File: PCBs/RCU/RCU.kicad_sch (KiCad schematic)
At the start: 0 parts

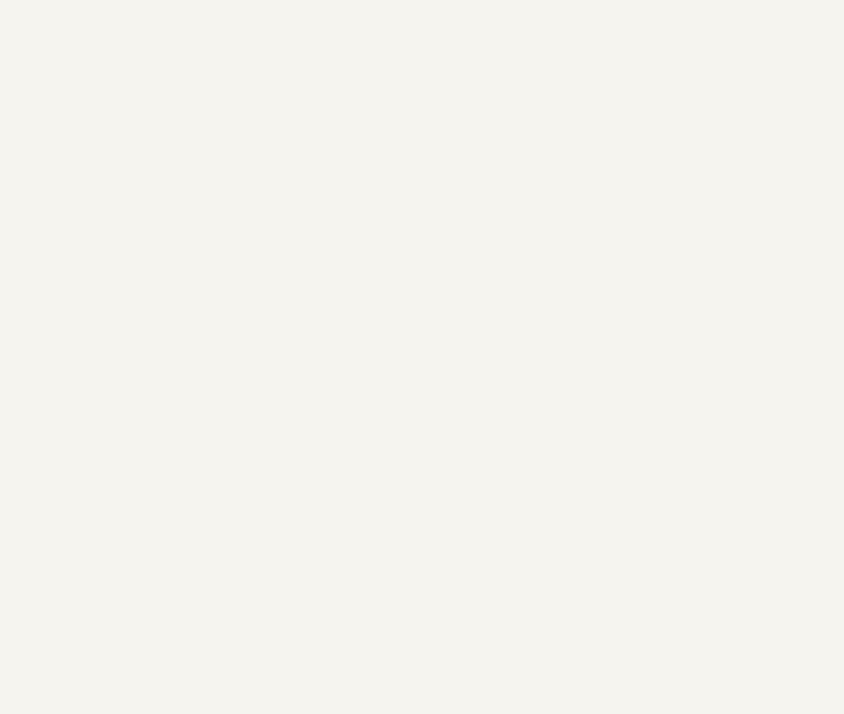
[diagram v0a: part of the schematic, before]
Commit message: Updated microcontroller schematic and created motor_control schematic
Changed all the net lables to global lavels except for NRST and USB_, added crystal resonator circuit, created DRV8876 symbol and added control signals to it
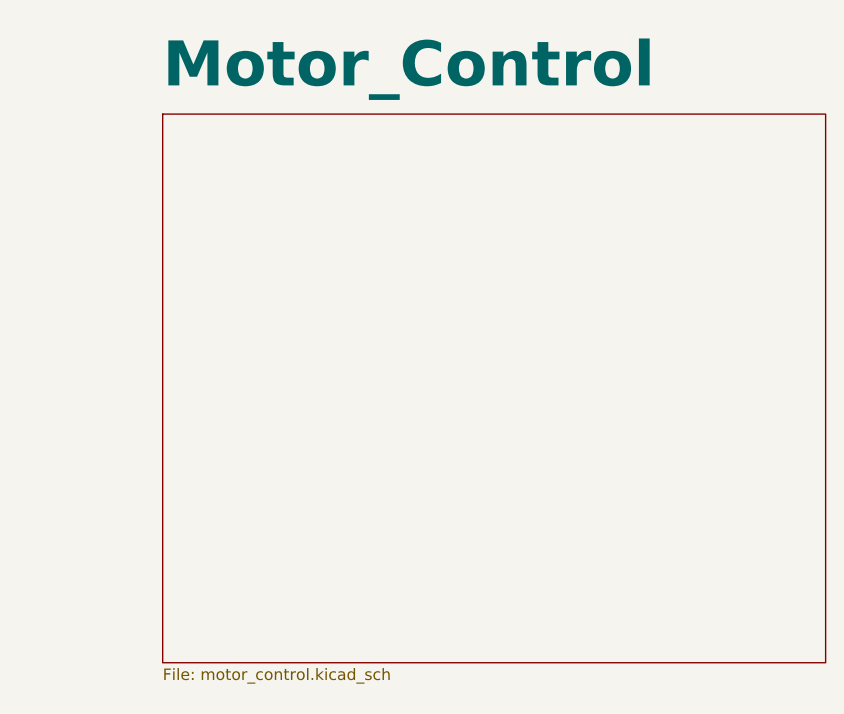
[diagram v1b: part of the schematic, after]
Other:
- added sheet Motor_Control (motor_control.kicad_sch)
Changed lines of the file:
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@@
 (kicad_sch (version 20211123) (generator eeschema)
   (paper "A4")
+  (sheet (at 139.7 26.67) (size 73.66 60.96) (fields_autoplaced)
+    (stroke (width 0.1524) (type solid) (color 0 0 0 0))
+    (fill (color 0 0 0 0.0000))
+    (property "Sheet name" "Motor_Control" (id 0) (at 139.7 24.0934 0)
+      (effects (font (size 5 5) bold) (justify left bottom))
+    )
+    (property "Sheet file" "motor_control.kicad_sch" (id 1) (at 139.7 88.2146 0)
+      (effects (font (size 1.27 1.27)) (justify left top))
+    )
+  )
   (sheet (at 33.7312 26.8732) (size 71.0184 61.722) (fields_autoplaced)
     (stroke (width 0.1524) (type solid) (color 0 0 0 0))
@@
     (path "/" (page "1"))
     (path "/c46a482e-bfa4-4ed5-a49f-3179709c39a1" (page "2"))
+    (path "/2537d888-fd78-4661-a6de-7d85959a9016" (page "3"))
   )
   (symbol_instances
+    (path "/c46a482e-bfa4-4ed5-a49f-3179709c39a1/8f435151-c909-4cdf-a7f9-67c1f7b1e16c"
+      (reference "#PWR?") (unit 1) (value "GND") (footprint "")
+    )
+    (path "/2537d888-fd78-4661-a6de-7d85959a9016/c8450c73-a493-44d4-8027-fc07076efa8b"
+      (reference "#PWR?") (unit 1) (value "GND") (footprint "")
+    )
+    (path "/2537d888-fd78-4661-a6de-7d85959a9016/d83684cc-8cc6-4e75-ba87-39c1c6e5d2a2"
+      (reference "#PWR?") (unit 1) (value "GND") (footprint "")
+    )
+    (path "/c46a482e-bfa4-4ed5-a49f-3179709c39a1/f4123535-8722-4c87-8b4b-05782cbf9e36"
+      (reference "#PWR?") (unit 1) (value "GND") (footprint "")
+    )
+    (path "/c46a482e-bfa4-4ed5-a49f-3179709c39a1/14fed118-9356-4bd7-9725-712b0ee562db"
+      (reference "C?") (unit 1) (value "C") (footprint "")
+    )
+    (path "/c46a482e-bfa4-4ed5-a49f-3179709c39a1/87164916-93ae-4140-86aa-59470124ec1a"
+      (reference "C?") (unit 1) (value "C") (footprint "")
+    )
+    (path "/c46a482e-bfa4-4ed5-a49f-3179709c39a1/f0f3dad0-df0a-4b6f-bcb1-cfd0a262d609"
+      (reference "R?") (unit 1) (value "R") (footprint "")
+    )
+    (path "/2537d888-fd78-4661-a6de-7d85959a9016/1574ac1c-14f2-474d-b3db-c10040047c62"
+      (reference "U?") (unit 1) (value "DRV8876") (footprint "")
+    )
     (path "/c46a482e-bfa4-4ed5-a49f-3179709c39a1/b6a46fb0-4feb-450f-9381-2291f852e487"
       (reference "U?") (unit 1) (value "STM32G0B1CBT6") (footprint "LQFP48_STM32G0B1CBT_STM")
     )
+    (path "/2537d888-fd78-4661-a6de-7d85959a9016/b8f09fbb-4af2-4957-adf9-6156648546de"
+      (reference "U?") (unit 1) (value "DRV8876") (footprint "")
+    )
+    (path "/c46a482e-bfa4-4ed5-a49f-3179709c39a1/65321985-657f-4e17-a0a5-f2f7935eae83"
+      (reference "Y?") (unit 1) (value "Crystal") (footprint "")
+    )
   )

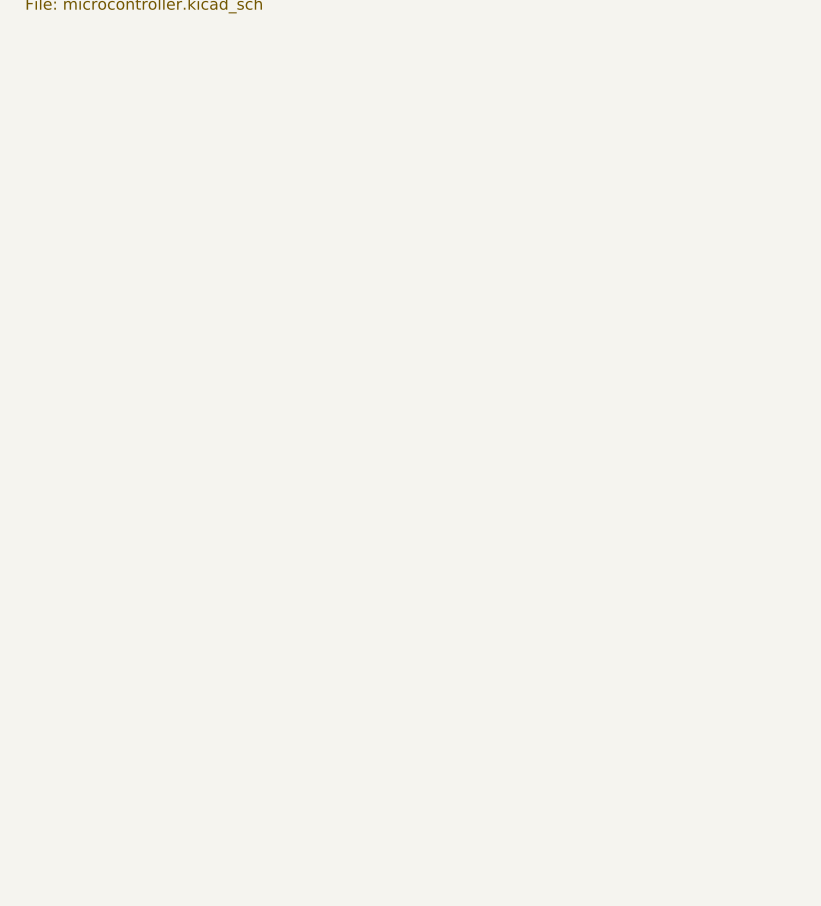
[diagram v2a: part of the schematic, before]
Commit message: Decided on Temperature_Humidity and Ambient Light Sensors
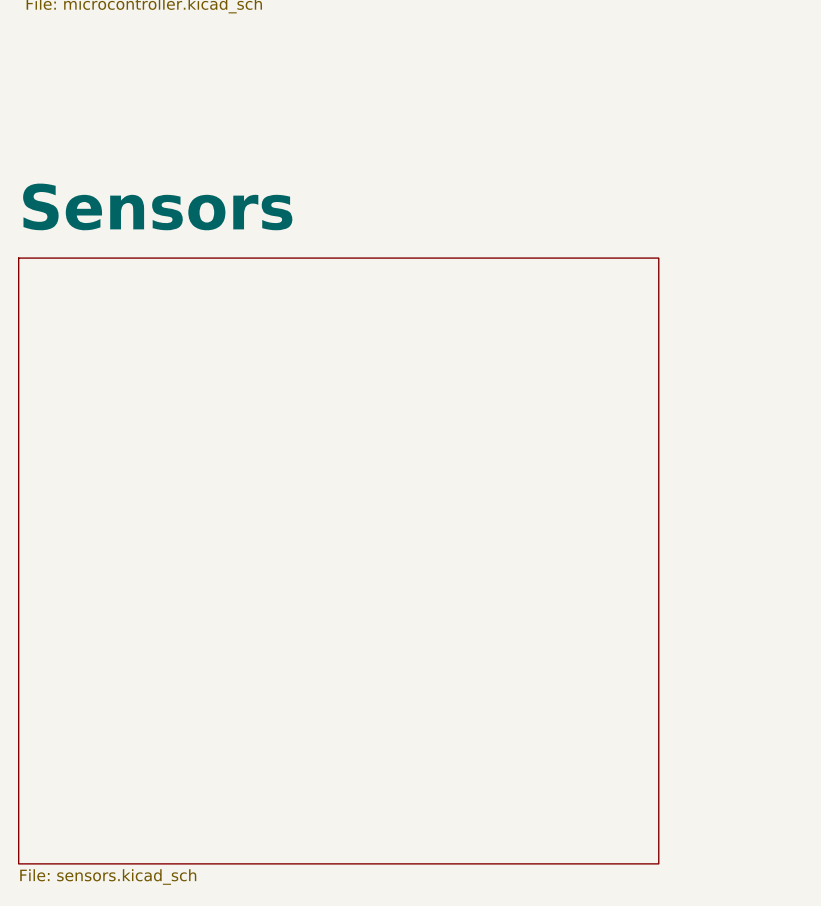
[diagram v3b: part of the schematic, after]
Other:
- added sheet Sensors (sensors.kicad_sch)
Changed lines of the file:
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@@
+    )
+  )
+  (sheet (at 33.02 118.11) (size 71.12 67.31) (fields_autoplaced)
+    (stroke (width 0.1524) (type solid) (color 0 0 0 0))
+    (fill (color 0 0 0 0.0000))
+    (property "Sheet name" "Sensors" (id 0) (at 33.02 115.5334 0)
+      (effects (font (size 5 5) bold) (justify left bottom))
+    )
+    (property "Sheet file" "sensors.kicad_sch" (id 1) (at 33.02 186.0046 0)
+      (effects (font (size 1.27 1.27)) (justify left top))
     )
   )
@@
     (path "/c46a482e-bfa4-4ed5-a49f-3179709c39a1" (page "2"))
     (path "/2537d888-fd78-4661-a6de-7d85959a9016" (page "3"))
+    (path "/6678d44b-178f-4b7c-833f-18a4e680f820" (page "4"))
   )
   (symbol_instances
     (path "/2537d888-fd78-4661-a6de-7d85959a9016/143e3232-b48c-44cf-9d6c-5d23f4f4f30d"
+      (reference "#PWR?") (unit 1) (value "+3.3V") (footprint "")
+    )
+    (path "/6678d44b-178f-4b7c-833f-18a4e680f820/1b7534fc-90ad-450a-b52b-2fcc0d68d4b9"
+      (reference "#PWR?") (unit 1) (value "GND") (footprint "")
+    )
+    (path "/6678d44b-178f-4b7c-833f-18a4e680f820/2f1ef7f6-3da7-40c6-9050-7587459efbf1"
       (reference "#PWR?") (unit 1) (value "+3.3V") (footprint "")
     )
@@
     (path "/2537d888-fd78-4661-a6de-7d85959a9016/4c1ec492-57a6-4f91-aeff-24a84fd4cbc5"
       (reference "#PWR?") (unit 1) (value "VCC") (footprint "")
+    )
+    (path "/6678d44b-178f-4b7c-833f-18a4e680f820/5469af30-69da-464c-a352-5a7564a6c776"
+      (reference "#PWR?") (unit 1) (value "GND") (footprint "")
     )
     (path "/2537d888-fd78-4661-a6de-7d85959a9016/5545570d-1f9a-4d13-950f-c87de7d5a636"
@@
     (path "/c46a482e-bfa4-4ed5-a49f-3179709c39a1/8f435151-c909-4cdf-a7f9-67c1f7b1e16c"
       (reference "#PWR?") (unit 1) (value "GND") (footprint "")
+    )
+    (path "/6678d44b-178f-4b7c-833f-18a4e680f820/96068ed0-4c2c-4cb9-9d68-483ed6507125"
+      (reference "#PWR?") (unit 1) (value "+3.3V") (footprint "")
     )
     (path "/2537d888-fd78-4661-a6de-7d85959a9016/ac6c9020-18df-42e7-9dbc-fa0e350749f6"
@@
       (reference "C") (unit 1) (value "22nF") (footprint "")
     )
+    (path "/6678d44b-178f-4b7c-833f-18a4e680f820/0bdd09eb-843d-4223-a9f9-fc632d0bcdb8"
+      (reference "C?") (unit 1) (value "1uF") (footprint "")
+    )
     (path "/c46a482e-bfa4-4ed5-a49f-3179709c39a1/14fed118-9356-4bd7-9725-712b0ee562db"
       (reference "C?") (unit 1) (value "C") (footprint "")
@@
       (reference "R?") (unit 1) (value "2.2k") (footprint "")
     )
+    (path "/6678d44b-178f-4b7c-833f-18a4e680f820/62ebd1cf-5b9b-4bab-92c2-efb41e0af239"
+      (reference "R?") (unit 1) (value "10k") (footprint "")
+    )
     (path "/2537d888-fd78-4661-a6de-7d85959a9016/6f117f6f-ff32-44da-a11c-21438911514e"
       (reference "R?") (unit 1) (value "2.2k") (footprint "")
@@
       (reference "U?") (unit 1) (value "DRV8876") (footprint "")
     )
+    (path "/6678d44b-178f-4b7c-833f-18a4e680f820/455511d5-40a2-4651-ab9c-da84f8d67b49"
+      (reference "U?") (unit 1) (value "SHT30-DIS") (footprint "Sensor_Humidity:Sensirion_DFN-8-1EP_2.5x2.5mm_P0.5mm_EP1.1x1.7mm")
+    )
+    (path "/6678d44b-178f-4b7c-833f-18a4e680f820/89bf4bbc-d6ea-4bfe-a92b-bb50d36c3083"
+      (reference "U?") (unit 1) (value "APDS-9306-065") (footprint "OptoDevice:Broadcom_DFN-6_2x2mm_P0.65mm")
+    )
     (path "/c46a482e-bfa4-4ed5-a49f-3179709c39a1/b6a46fb0-4feb-450f-9381-2291f852e487"
